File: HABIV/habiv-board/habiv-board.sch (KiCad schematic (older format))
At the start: 119 parts, among them IC1 RTC_PCF8523T, J1 Micro_SD_Card_Det, J10 Conn_01x02_Female, J11 Conn_01x02_Female, J12 Conn_01x02_Female, J13 Conn_01x02_Female, J14 Conn_01x02_Female, J15 Conn_01x02_Female, J16 Conn_01x02_Female, J2 Conn_ARM_JTAG_SWD_20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

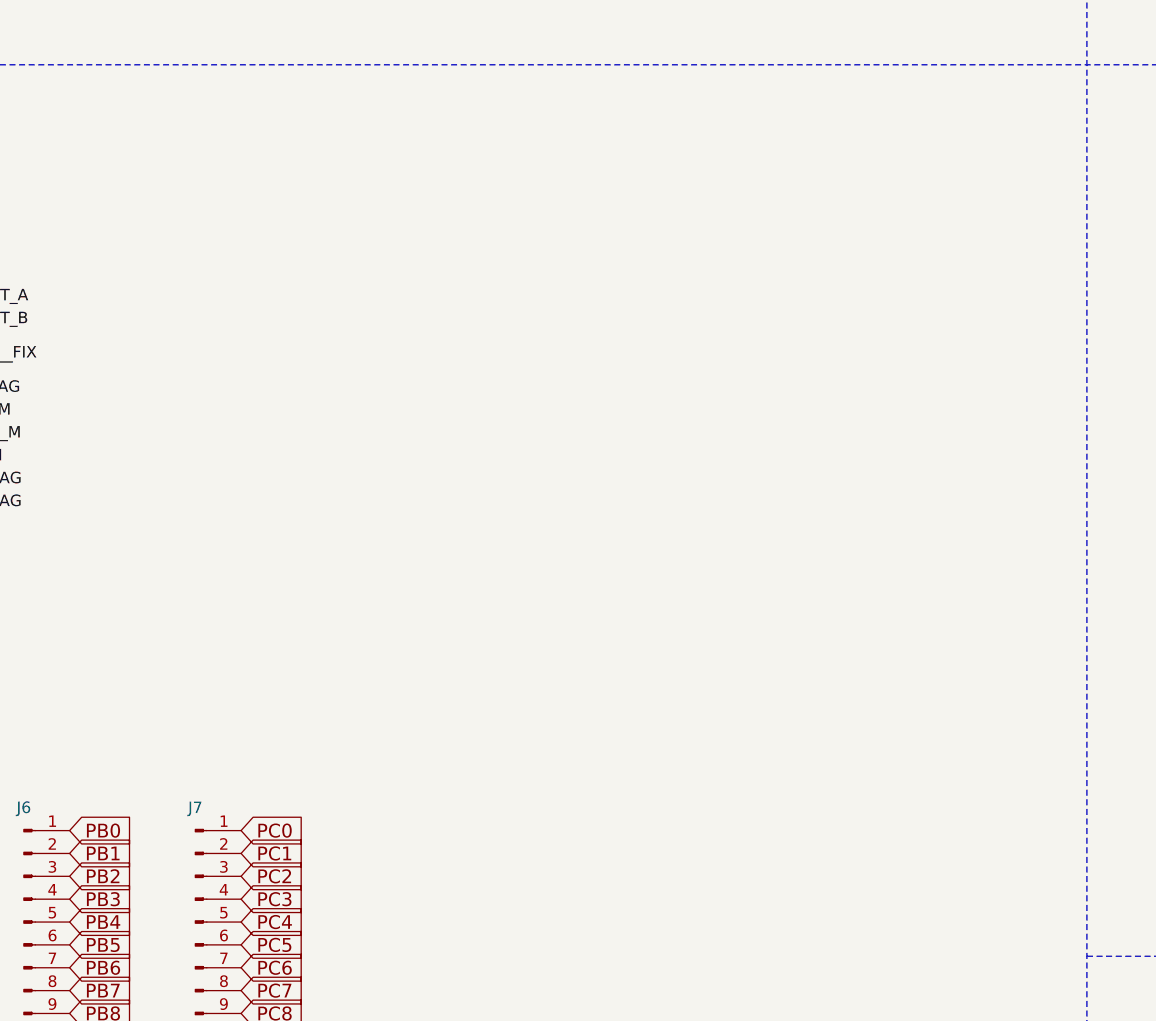
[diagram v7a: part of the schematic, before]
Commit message: add servo breakouts
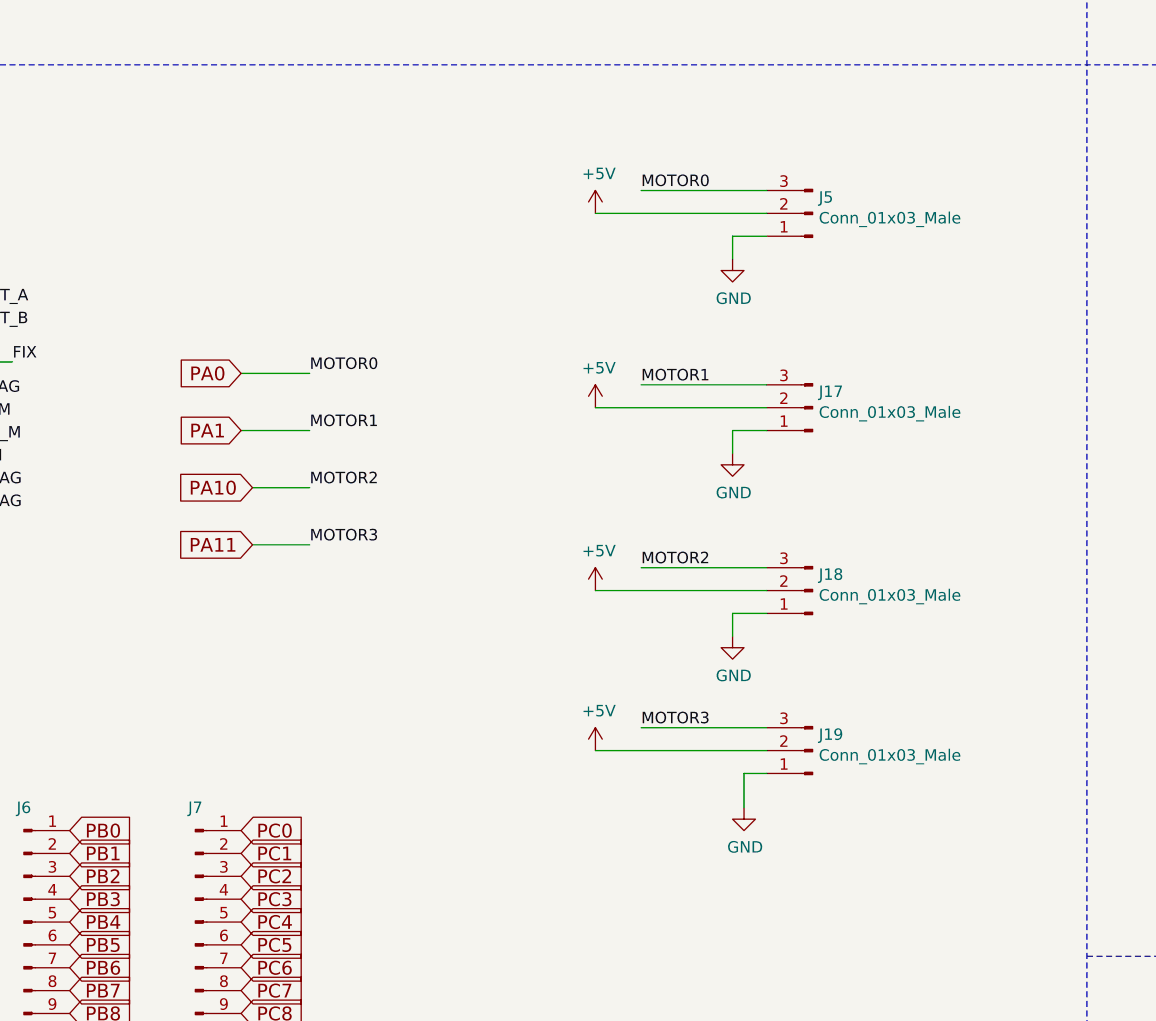
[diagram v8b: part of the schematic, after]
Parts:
- added J17, J18, J19, J5: Conn_01x03_Male, Connector_PinHeader_2.54mm:PinHeader_1x03_P2.54mm_Vertical, symbol Connector:Conn_01x03_Male
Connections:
- net +5V: now also J17.2 (Pin_2), J18.2 (Pin_2), J19.2 (Pin_2), J5.2 (Pin_2)
- net GND: now also J17.1 (Pin_1), J18.1 (Pin_1), J19.1 (Pin_1), J5.1 (Pin_1)
- net PA0: now also J5.3 (Pin_3)
- net PA1: now also J17.3 (Pin_3)
- net PA10: now also J18.3 (Pin_3)
- net PA11: now also J19.3 (Pin_3)
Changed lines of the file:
@@
 Wire Wire Line
 	15400 5900 15600 5900
+Text GLabel 10550 6400 0    60   Input ~ 0
+PA11
+Text GLabel 10550 6150 0    60   Input ~ 0
+PA10
+Text GLabel 10500 5650 0    60   Input ~ 0
+PA0
+Text GLabel 10500 5900 0    60   Input ~ 0
+PA1
+Wire Wire Line
+	10500 5650 10800 5650
+Wire Wire Line
+	10500 5900 10800 5900
+Wire Wire Line
+	10550 6150 10800 6150
+Wire Wire Line
+	10550 6400 10800 6400
+Text Label 10800 5650 0    50   ~ 0
+MOTOR0
+Text Label 10800 5900 0    50   ~ 0
+MOTOR1
+Text Label 10800 6150 0    50   ~ 0
+MOTOR2
+Text Label 10800 6400 0    50   ~ 0
+MOTOR3
+Text Label 12250 4850 0    50   ~ 0
+MOTOR0
+Text Label 12250 5700 0    50   ~ 0
+MOTOR1
+Text Label 12250 6500 0    50   ~ 0
+MOTOR2
+Text Label 12250 7200 0    50   ~ 0
+MOTOR3
+$Comp
+L Connector:Conn_01x03_Male J5
+U 1 1 5D268449
+P 13000 4950
+F 0 "J5" H 12973 4880 50  0000 R CNN
+F 1 "Conn_01x03_Male" H 12973 4971 50  0000 R CNN
+F 2 "Connector_PinHeader_2.54mm:PinHeader_1x03_P2.54mm_Vertical" H 13000 4950 50  0001 C CNN
+F 3 "~" H 13000 4950 50  0001 C CNN
+	1    13000 4950
+	-1   0    0    1
+$EndComp
+$Comp
+L Connector:Conn_01x03_Male J17
+U 1 1 5D2687A6
+P 13000 5800
+F 0 "J17" H 12973 5730 50  0000 R CNN
+F 1 "Conn_01x03_Male" H 12973 5821 50  0000 R CNN
+F 2 "Connector_PinHeader_2.54mm:PinHeader_1x03_P2.54mm_Vertical" H 13000 5800 50  0001 C CNN
+F 3 "~" H 13000 5800 50  0001 C CNN
+	1    13000 5800
+	-1   0    0    1
+$EndComp
+$Comp
+L Connector:Conn_01x03_Male J18
+U 1 1 5D268A46
+P 13000 6600
+F 0 "J18" H 12973 6530 50  0000 R CNN
+F 1 "Conn_01x03_Male" H 12973 6621 50  0000 R CNN
+F 2 "Connector_PinHeader_2.54mm:PinHeader_1x03_P2.54mm_Vertical" H 13000 6600 50  0001 C CNN
+F 3 "~" H 13000 6600 50  0001 C CNN
+	1    13000 6600
+	-1   0    0    1
+$EndComp
+$Comp
+L Connector:Conn_01x03_Male J19
+U 1 1 5D268CE1
+P 13000 7300
+F 0 "J19" H 12973 7230 50  0000 R CNN
+F 1 "Conn_01x03_Male" H 12973 7321 50  0000 R CNN
+F 2 "Connector_PinHeader_2.54mm:PinHeader_1x03_P2.54mm_Vertical" H 13000 7300 50  0001 C CNN
+F 3 "~" H 13000 7300 50  0001 C CNN
+	1    13000 7300
+	-1   0    0    1
+$EndComp
+Wire Wire Line
+	12250 4850 12800 4850
+Wire Wire Line
+	12250 5700 12800 5700
+Wire Wire Line
+	12250 6500 12800 6500
+Wire Wire Line
+	12250 7200 12800 7200
+$Comp
+L power:+5V #PWR0115
+U 1 1 5DA8AB00
+P 12050 4950
+F 0 "#PWR0115" H 12050 4800 50  0001 C CNN
+F 1 "+5V" H 12065 5123 50  0000 C CNN
+F 2 "" H 12050 4950 50  0001 C CNN
+F 3 "" H 12050 4950 50  0001 C CNN
+	1    12050 4950
+	1    0    0    -1
+$EndComp
+$Comp
+L power:+5V #PWR0116
+U 1 1 5DA8B9DD
+P 12050 5800
+F 0 "#PWR0116" H 12050 5650 50  0001 C CNN
+F 1 "+5V" H 12065 5973 50  0000 C CNN
+F 2 "" H 12050 5800 50  0001 C CNN
+F 3 "" H 12050 5800 50  0001 C CNN
+	1    12050 5800
+	1    0    0    -1
+$EndComp
+$Comp
+L power:+5V #PWR0117
+U 1 1 5DAC4222
+P 12050 6600
+F 0 "#PWR0117" H 12050 6450 50  0001 C CNN
+F 1 "+5V" H 12065 6773 50  0000 C CNN
+F 2 "" H 12050 6600 50  0001 C CNN
+F 3 "" H 12050 6600 50  0001 C CNN
+	1    12050 6600
+	1    0    0    -1
+$EndComp
+$Comp
+L power:+5V #PWR0118
+U 1 1 5DAFC524
+P 12050 7300
+F 0 "#PWR0118" H 12050 7150 50  0001 C CNN
+F 1 "+5V" H 12065 7473 50  0000 C CNN
+F 2 "" H 12050 7300 50  0001 C CNN
+F 3 "" H 12050 7300 50  0001 C CNN
+	1    12050 7300
+	1    0    0    -1
+$EndComp
+Wire Wire Line
+	12050 4950 12800 4950
+Wire Wire Line
+	12050 5800 12800 5800
+Wire Wire Line
+	12050 6600 12800 6600
+Wire Wire Line
+	12050 7300 12800 7300
+$Comp
+L power:GND #PWR0119
+U 1 1 5DF5FC36
+P 12700 7550
+F 0 "#PWR0119" H 12700 7300 50  0001 C CNN
+F 1 "GND" H 12705 7377 50  0000 C CNN
+F 2 "" H 12700 7550 50  0001 C CNN
+F 3 "" H 12700 7550 50  0001 C CNN
+	1    12700 7550
+	1    0    0    -1
+$EndComp
+Wire Wire Line
+	12700 7550 12700 7400
+Wire Wire Line
+	12700 7400 12800 7400
+$Comp
+L power:GND #PWR0120
+U 1 1 5DF9A30C
+P 12650 6000
+F 0 "#PWR0120" H 12650 5750 50  0001 C CNN
+F 1 "GND" H 12655 5827 50  0000 C CNN
+F 2 "" H 12650 6000 50  0001 C CNN
+F 3 "" H 12650 6000 50  0001 C CNN
+	1    12650 6000
+	1    0    0    -1
+$EndComp
+Wire Wire Line
+	12650 6000 12650 5900
+Wire Wire Line
+	12650 5900 12800 5900
+$Comp
+L power:GND #PWR0121
+U 1 1 5DFD75A3
+P 12650 5150
+F 0 "#PWR0121" H 12650 4900 50  0001 C CNN
+F 1 "GND" H 12655 4977 50  0000 C CNN
+F 2 "" H 12650 5150 50  0001 C CNN
+F 3 "" H 12650 5150 50  0001 C CNN
+	1    12650 5150
+	1    0    0    -1
+$EndComp
+Wire Wire Line
+	12650 5150 12650 5050
+Wire Wire Line
+	12650 5050 12800 5050
+$Comp
+L power:GND #PWR0122
+U 1 1 5E012C13
+P 12650 6800
+F 0 "#PWR0122" H 12650 6550 50  0001 C CNN
+F 1 "GND" H 12655 6627 50  0000 C CNN
+F 2 "" H 12650 6800 50  0001 C CNN
+F 3 "" H 12650 6800 50  0001 C CNN
+	1    12650 6800
+	1    0    0    -1
+$EndComp
+Wire Wire Line
+	12650 6800 12650 6700
+Wire Wire Line
+	12650 6700 12800 6700
 $EndSCHEMATC
